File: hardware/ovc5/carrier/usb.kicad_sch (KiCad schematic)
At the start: 98 parts, among them J1 USB_C_Receptacle, U10 S25FL064, U2 CYUSB43x7, U5 USB3_A_Dual_Stacked, U8 TPS2561, Y1 25MHz

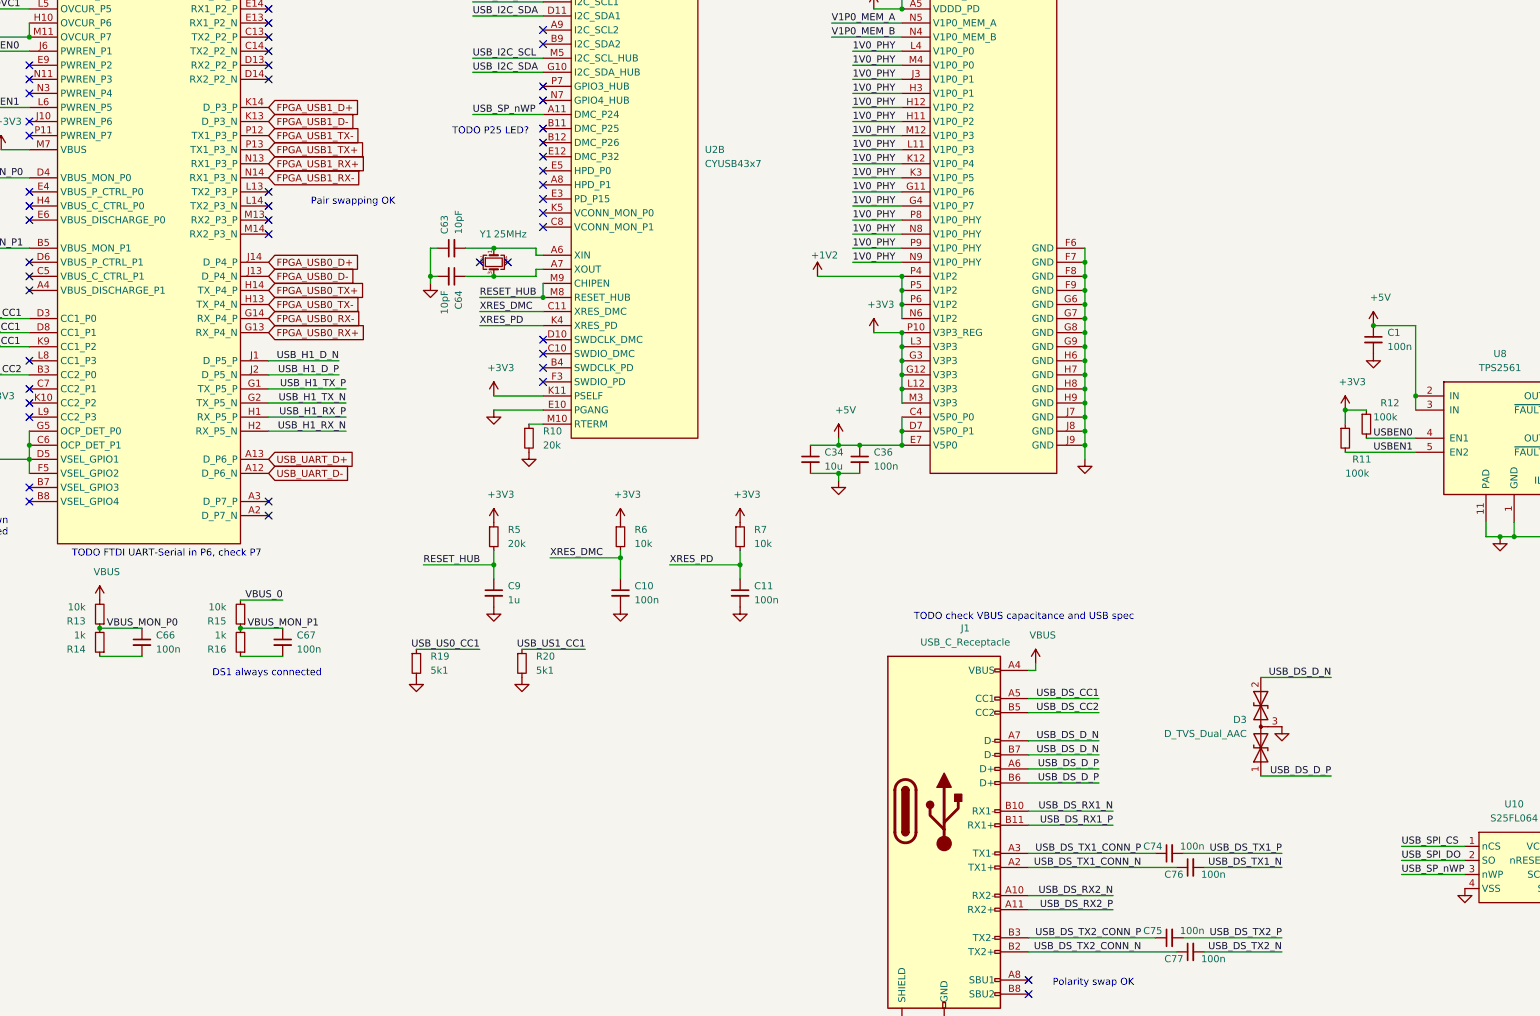
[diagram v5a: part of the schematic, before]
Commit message: Routing and FPGA pin assignment optimizations
Also fixed some pins that were NC by accident

Signed-off-by: Luca Della Vedova <luca@openrobotics.org>
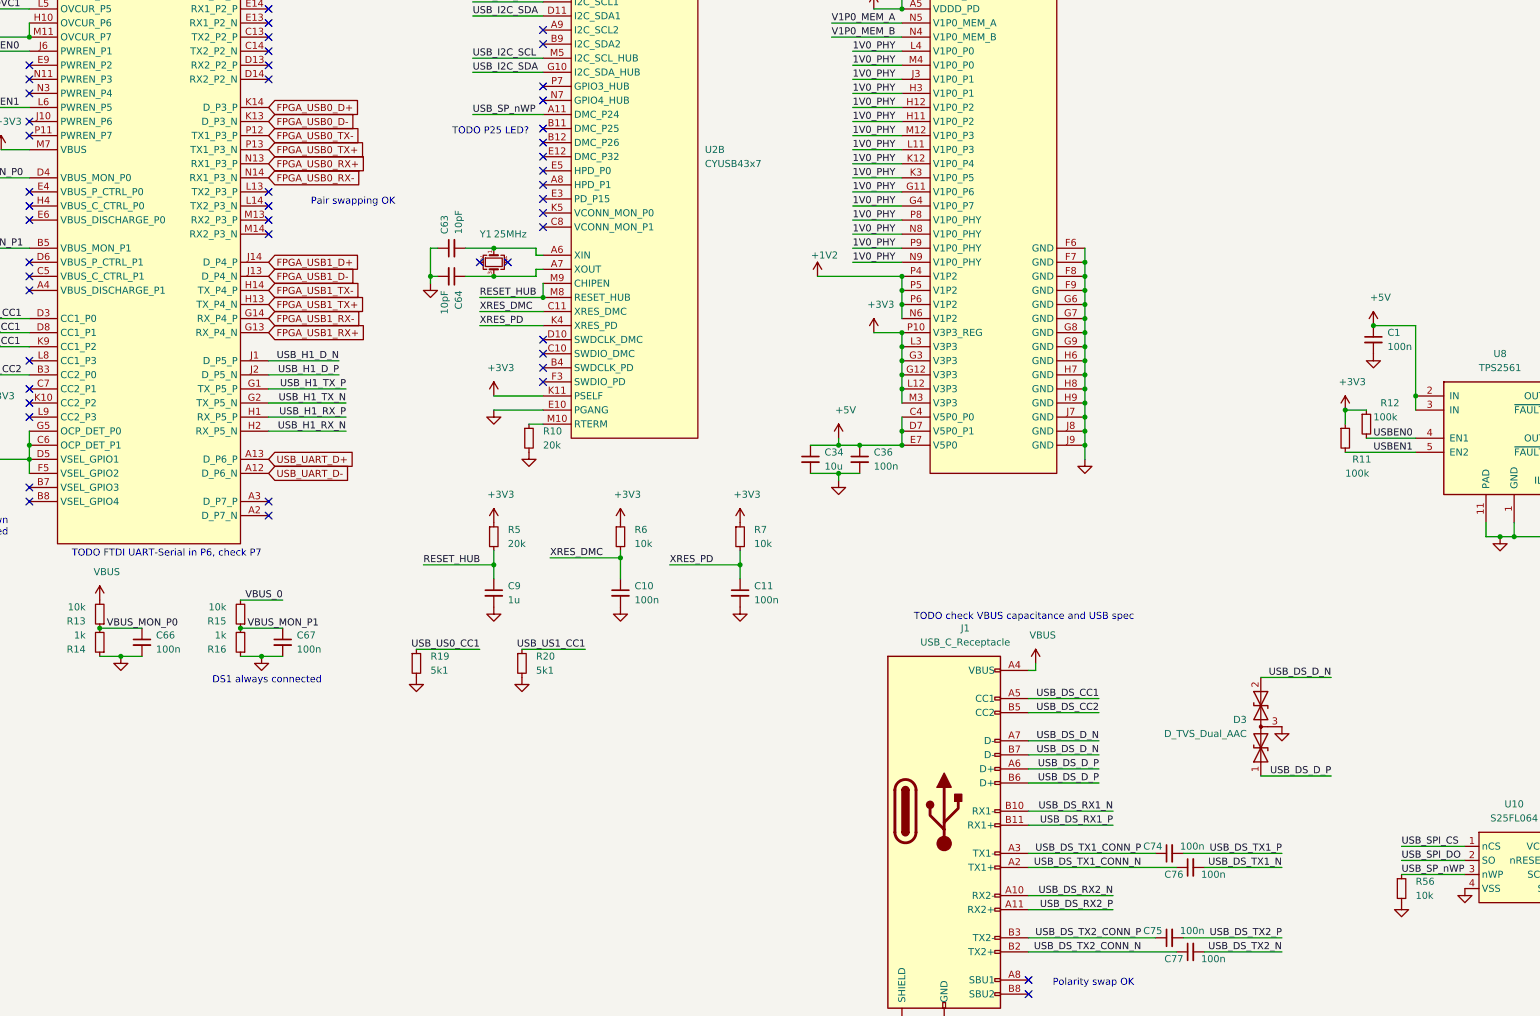
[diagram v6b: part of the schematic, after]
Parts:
- added R56: 10k, Resistor_SMD:R_0402_1005Metric, symbol Device:R_Small
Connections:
- net FPGA_USB0_D+: now also U2.K14 (D_P3_P); no longer U2.J14 (D_P4_P)
- net FPGA_USB0_D-: now also U2.K13 (D_P3_N); no longer U2.J13 (D_P4_N)
- net FPGA_USB0_RX+: now also U2.N13 (RX1_P3_P); no longer U2.G13 (RX_P4_N)
- net FPGA_USB0_RX-: now also U2.N14 (RX1_P3_N); no longer U2.G14 (RX_P4_P)
- net FPGA_USB0_TX+: now also U2.P13 (TX1_P3_N); no longer U2.H14 (TX_P4_P)
- net FPGA_USB0_TX-: now also U2.P12 (TX1_P3_P); no longer U2.H13 (TX_P4_N)
- net FPGA_USB1_D+: now also U2.J14 (D_P4_P); no longer U2.K14 (D_P3_P)
- net FPGA_USB1_D-: now also U2.J13 (D_P4_N); no longer U2.K13 (D_P3_N)
- net FPGA_USB1_RX+: now also U2.G13 (RX_P4_N); no longer U2.N13 (RX1_P3_P)
- net FPGA_USB1_RX-: now also U2.G14 (RX_P4_P); no longer U2.N14 (RX1_P3_N)
- net FPGA_USB1_TX+: now also U2.H13 (TX_P4_N); no longer U2.P13 (TX1_P3_N)
- net FPGA_USB1_TX-: now also U2.H14 (TX_P4_P); no longer U2.P12 (TX1_P3_P)
- net GND: now also C66.2, C67.2, R14.1, R16.1, R56.2
- net USB_SP_nWP: now also R56.1
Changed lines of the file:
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@@
   (junction (at 12.7 154.94) (diameter 0.9144) (color 0 0 0 0))
   (junction (at 25.4 185.42) (diameter 0.9144) (color 0 0 0 0))
+  (junction (at 29.21 190.5) (diameter 0.9144) (color 0 0 0 0))
   (junction (at 41.91 -5.08) (diameter 0.9144) (color 0 0 0 0))
   (junction (at 41.91 0) (diameter 0.9144) (color 0 0 0 0))
@@
   (junction (at 50.8 0) (diameter 0.9144) (color 0 0 0 0))
   (junction (at 50.8 185.42) (diameter 0.9144) (color 0 0 0 0))
+  (junction (at 54.61 190.5) (diameter 0.9144) (color 0 0 0 0))
   (junction (at 59.69 -5.08) (diameter 0.9144) (color 0 0 0 0))
   (junction (at 59.69 0) (diameter 0.9144) (color 0 0 0 0))
@@
     (stroke (width 0) (type solid) (color 0 0 0 0))
   )
-  (wire (pts (xy 25.4 190.5) (xy 33.02 190.5))
+  (wire (pts (xy 25.4 190.5) (xy 29.21 190.5))
+    (stroke (width 0) (type solid) (color 0 0 0 0))
+  )
+  (wire (pts (xy 29.21 190.5) (xy 33.02 190.5))
     (stroke (width 0) (type solid) (color 0 0 0 0))
   )
@@
     (stroke (width 0) (type solid) (color 0 0 0 0))
   )
-  (wire (pts (xy 50.8 190.5) (xy 58.42 190.5))
+  (wire (pts (xy 50.8 190.5) (xy 54.61 190.5))
+    (stroke (width 0) (type solid) (color 0 0 0 0))
+  )
+  (wire (pts (xy 54.61 190.5) (xy 58.42 190.5))
     (stroke (width 0) (type solid) (color 0 0 0 0))
   )
@@
     (effects (font (size 1.27 1.27)) (justify right bottom))
   )
-  (text "DS1 always connected" (at 45.72 194.31 0)
+  (text "DS1 always connected" (at 45.72 195.58 0)
     (effects (font (size 1.27 1.27)) (justify left bottom))
   )
@@
     (effects (font (size 1.27 1.27)) (justify right bottom))
   )
-  (global_label "FPGA_USB1_D+" (shape input) (at 55.88 91.44 0)
+  (global_label "FPGA_USB0_D+" (shape input) (at 55.88 91.44 0)
     (effects (font (size 1.27 1.27)) (justify left))
     (property "Intersheet References" "${INTERSHEET_REFS}" (id 0) (at 72.8074 91.5194 0)
@@
     )
   )
-  (global_label "FPGA_USB1_D-" (shape input) (at 55.88 93.98 0)
+  (global_label "FPGA_USB0_D-" (shape input) (at 55.88 93.98 0)
     (effects (font (size 1.27 1.27)) (justify left))
     (property "Intersheet References" "${INTERSHEET_REFS}" (id 0) (at 72.8074 94.0594 0)
@@
     )
   )
-  (global_label "FPGA_USB1_TX-" (shape input) (at 55.88 96.52 0)
+  (global_label "FPGA_USB0_TX-" (shape input) (at 55.88 96.52 0)
     (effects (font (size 1.27 1.27)) (justify left))
     (property "Intersheet References" "${INTERSHEET_REFS}" (id 0) (at 73.7145 96.5994 0)
@@
     )
   )
-  (global_label "FPGA_USB1_TX+" (shape input) (at 55.88 99.06 0)
+  (global_label "FPGA_USB0_TX+" (shape input) (at 55.88 99.06 0)
     (effects (font (size 1.27 1.27)) (justify left))
     (property "Intersheet References" "${INTERSHEET_REFS}" (id 0) (at 73.7145 99.1394 0)
@@
     )
   )
-  (global_label "FPGA_USB1_RX+" (shape input) (at 55.88 101.6 0)
+  (global_label "FPGA_USB0_RX+" (shape input) (at 55.88 101.6 0)
     (effects (font (size 1.27 1.27)) (justify left))
     (property "Intersheet References" "${INTERSHEET_REFS}" (id 0) (at 74.0169 101.5206 0)
@@
     )
   )
-  (global_label "FPGA_USB1_RX-" (shape input) (at 55.88 104.14 0)
+  (global_label "FPGA_USB0_RX-" (shape input) (at 55.88 104.14 0)
     (effects (font (size 1.27 1.27)) (justify left))
     (property "Intersheet References" "${INTERSHEET_REFS}" (id 0) (at 74.0169 104.0606 0)
@@
     )
   )
-  (global_label "FPGA_USB0_D+" (shape input) (at 55.88 119.38 0)
+  (global_label "FPGA_USB1_D+" (shape input) (at 55.88 119.38 0)
     (effects (font (size 1.27 1.27)) (justify left))
     (property "Intersheet References" "${INTERSHEET_REFS}" (id 0) (at 72.8074 119.4594 0)
@@
     )
   )
-  (global_label "FPGA_USB0_D-" (shape input) (at 55.88 121.92 0)
+  (global_label "FPGA_USB1_D-" (shape input) (at 55.88 121.92 0)
     (effects (font (size 1.27 1.27)) (justify left))
     (property "Intersheet References" "${INTERSHEET_REFS}" (id 0) (at 72.8074 121.9994 0)
@@
     )
   )
-  (global_label "FPGA_USB0_TX+" (shape input) (at 55.88 124.46 0)
+  (global_label "FPGA_USB1_TX-" (shape input) (at 55.88 124.46 0)
     (effects (font (size 1.27 1.27)) (justify left))
     (property "Intersheet References" "${INTERSHEET_REFS}" (id 0) (at 73.7145 124.5394 0)
@@
     )
   )
-  (global_label "FPGA_USB0_TX-" (shape input) (at 55.88 127 0)
+  (global_label "FPGA_USB1_TX+" (shape input) (at 55.88 127 0)
     (effects (font (size 1.27 1.27)) (justify left))
     (property "Intersheet References" "${INTERSHEET_REFS}" (id 0) (at 73.7145 127.0794 0)
@@
     )
   )
-  (global_label "FPGA_USB0_RX-" (shape input) (at 55.88 129.54 0)
+  (global_label "FPGA_USB1_RX-" (shape input) (at 55.88 129.54 0)
     (effects (font (size 1.27 1.27)) (justify left))
     (property "Intersheet References" "${INTERSHEET_REFS}" (id 0) (at 74.0169 129.4606 0)
@@
     )
   )
-  (global_label "FPGA_USB0_RX+" (shape input) (at 55.88 132.08 0)
+  (global_label "FPGA_USB1_RX+" (shape input) (at 55.88 132.08 0)
     (effects (font (size 1.27 1.27)) (justify left))
     (property "Intersheet References" "${INTERSHEET_REFS}" (id 0) (at 74.0169 132.0006 0)
@@
     (pin "1")
   )
+  (symbol (lib_id "power:GND") (at 29.21 190.5 0) (unit 1)
+    (in_bom yes) (on_board yes)
+    (property "Reference" "#PWR0375" (id 0) (at 29.21 196.85 0)
+      (effects (font (size 1.27 1.27)) hide)
+    )
+    (property "Value" "GND" (id 1) (at 30.48 195.58 0)
+      (effects (font (size 1.27 1.27)) hide)
+    )
+    (property "Footprint" "" (id 2) (at 29.21 190.5 0)
+      (effects (font (size 1.27 1.27)) hide)
+    )
+    (property "Datasheet" "" (id 3) (at 29.21 190.5 0)
+      (effects (font (size 1.27 1.27)) hide)
+    )
+    (pin "1")
+  )
+  (symbol (lib_id "power:GND") (at 54.61 190.5 0) (unit 1)
+    (in_bom yes) (on_board yes)
+    (property "Reference" "#PWR0376" (id 0) (at 54.61 196.85 0)
+      (effects (font (size 1.27 1.27)) hide)
+    )
+    (property "Value" "GND" (id 1) (at 55.88 195.58 0)
+      (effects (font (size 1.27 1.27)) hide)
+    )
+    (property "Footprint" "" (id 2) (at 54.61 190.5 0)
+      (effects (font (size 1.27 1.27)) hide)
+    )
+    (property "Datasheet" "" (id 3) (at 54.61 190.5 0)
+      (effects (font (size 1.27 1.27)) hide)
+    )
+    (pin "1")
+  )
   (symbol (lib_id "power:GND") (at 82.55 194.31 0) (unit 1)
     (in_bom yes) (on_board yes)
@@
     (pin "1")
   )
+  (symbol (lib_id "power:GND") (at 260.35 234.95 0) (unit 1)
+    (in_bom yes) (on_board yes)
+    (property "Reference" "#PWR0379" (id 0) (at 260.35 241.3 0)
+      (effects (font (size 1.27 1.27)) hide)
+    )
+    (property "Value" "GND" (id 1) (at 261.62 240.03 0)
+      (effects (font (size 1.27 1.27)) hide)
+    )
+    (property "Footprint" "" (id 2) (at 260.35 234.95 0)
+      (effects (font (size 1.27 1.27)) hide)
+    )
+    (property "Datasheet" "" (id 3) (at 260.35 234.95 0)
+      (effects (font (size 1.27 1.27)) hide)
+    )
+    (pin "1")
+  )
   (symbol (lib_id "power:GND") (at 271.78 232.41 0) (unit 1)
     (in_bom yes) (on_board yes)
@@
       (effects (font (size 1.27 1.27)) hide)
     )
+    (pin "1")
+    (pin "2")
+  )
+  (symbol (lib_id "Device:R_Small") (at 260.35 232.41 0) (unit 1)
+    (in_bom yes) (on_board yes)
+    (property "Reference" "R56" (id 0) (at 262.89 231.14 0)
+      (effects (font (size 1.27 1.27)) (justify left))
+    )
+    (property "Value" "10k" (id 1) (at 262.89 233.68 0)
+      (effects (font (size 1.27 1.27)) (justify left))
+    )
+    (property "Footprint" "Resistor_SMD:R_0402_1005Metric" (id 2) (at 260.35 232.41 0)
+      (effects (font (size 1.27 1.27)) hide)
+    )
+    (property "Datasheet" "~" (id 3) (at 260.35 232.41 0)
+      (effects (font (size 1.27 1.27)) hide)
+    )
+    (property "D1N" "Digikey" (id 4) (at 260.35 232.41 0)
+      (effects (font (size 1.27 1.27)) hide)
+    )
+    (property "D1PN" "YAG3436CT-ND" (id 5) (at 260.35 232.41 0)
+      (effects (font (size 1.27 1.27)) hide)
+    )
+    (property "MFN" "Yageo" (id 6) (at 260.35 232.41 0)
+      (effects (font (size 1.27 1.27)) hide)
+    )
+    (property "MPN" "AC0402FR-0710KL" (id 7) (at 260.35 232.41 0)
+      (effects (font (size 1.27 1.27)) hide)
+    )

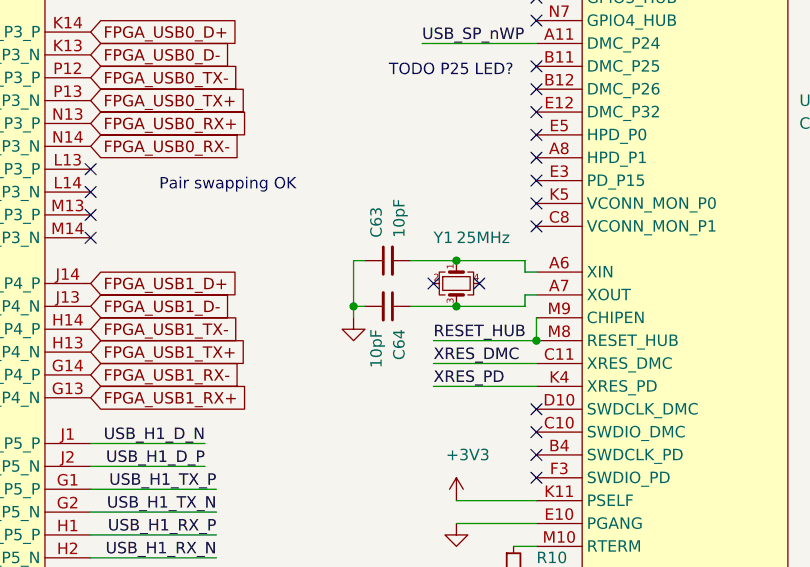
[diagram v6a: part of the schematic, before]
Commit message: Address feedback
Fix oscillator circuit
Fix skew in MIPI lane

Signed-off-by: Luca Della Vedova <luca@openrobotics.org>
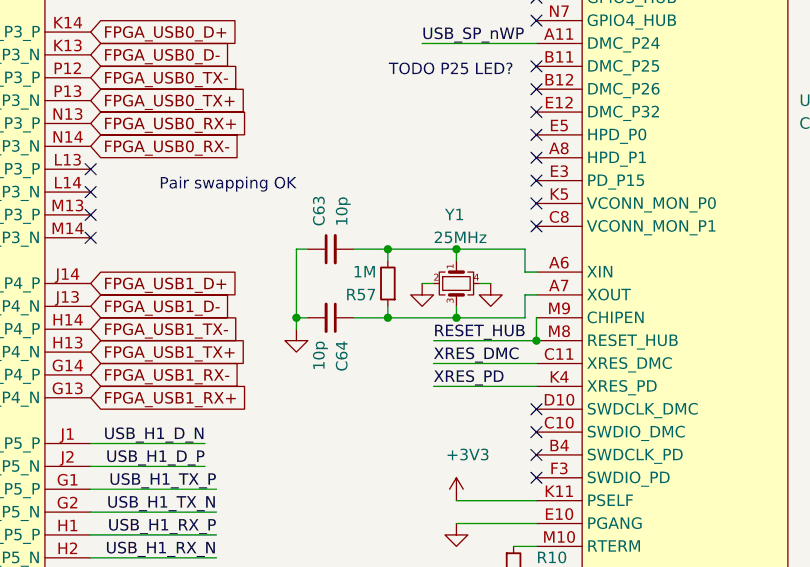
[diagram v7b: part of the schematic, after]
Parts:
- added R57: 1M, Resistor_SMD:R_0402_1005Metric, symbol Device:R_Small
- C63, C64: value 10pF -> 10p
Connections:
- net GND: now also Y1.2, Y1.4
- net at C63.2, U2.A6 (XIN), Y1.1: now also R57.2
- net at C64.1, U2.A7 (XOUT), Y1.3: now also R57.1
- no-connect marks 58 -> 56
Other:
- moved on the sheet: C63, C64
